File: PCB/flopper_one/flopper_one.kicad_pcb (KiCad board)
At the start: 2 copper layers, 78 x 61 mm, 13 parts, among them J1 To PN532 ->, J2 <- ST7789, Q1 2N2219, SW1 SW_Omron_B3FS, SW2 SW_Omron_B3FS, SW3 SW_Omron_B3FS, SW4 SW_Omron_B3FS, SW5 SW_Omron_B3FS

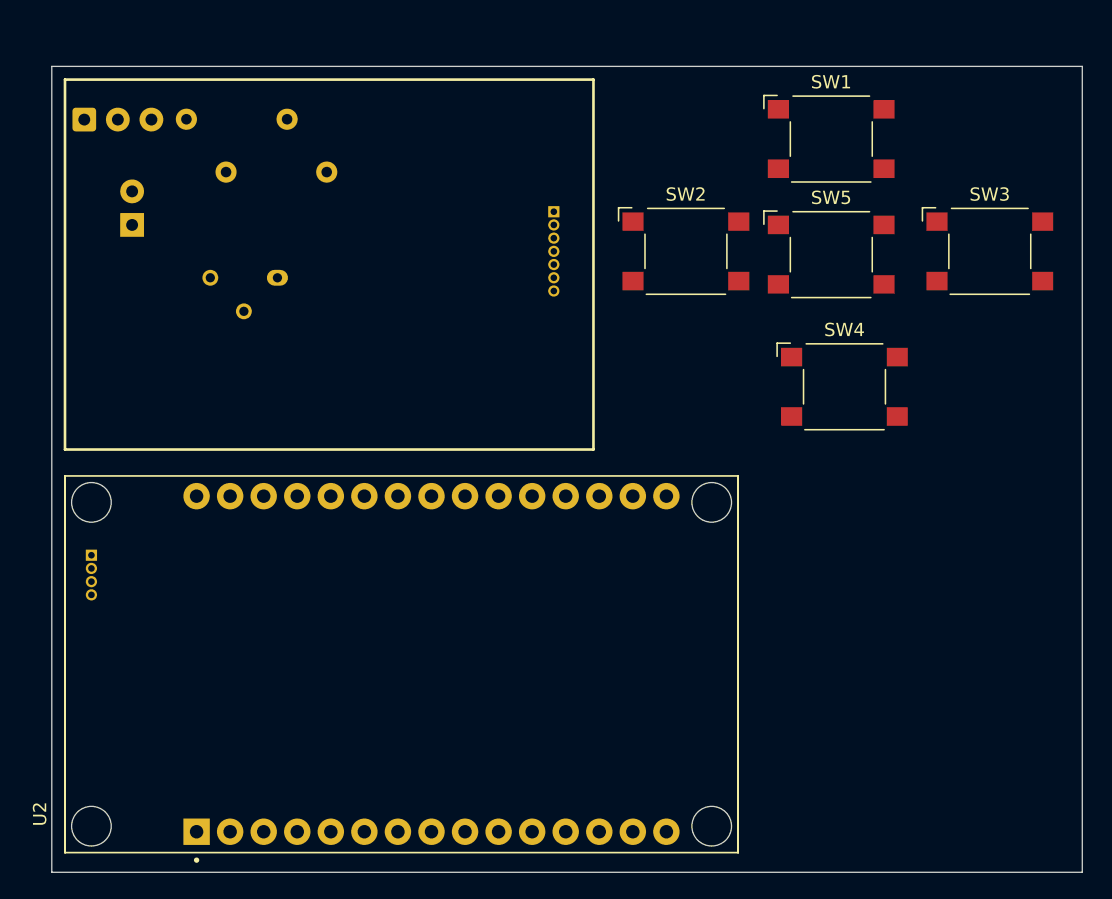
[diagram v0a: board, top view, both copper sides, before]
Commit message: routed switches
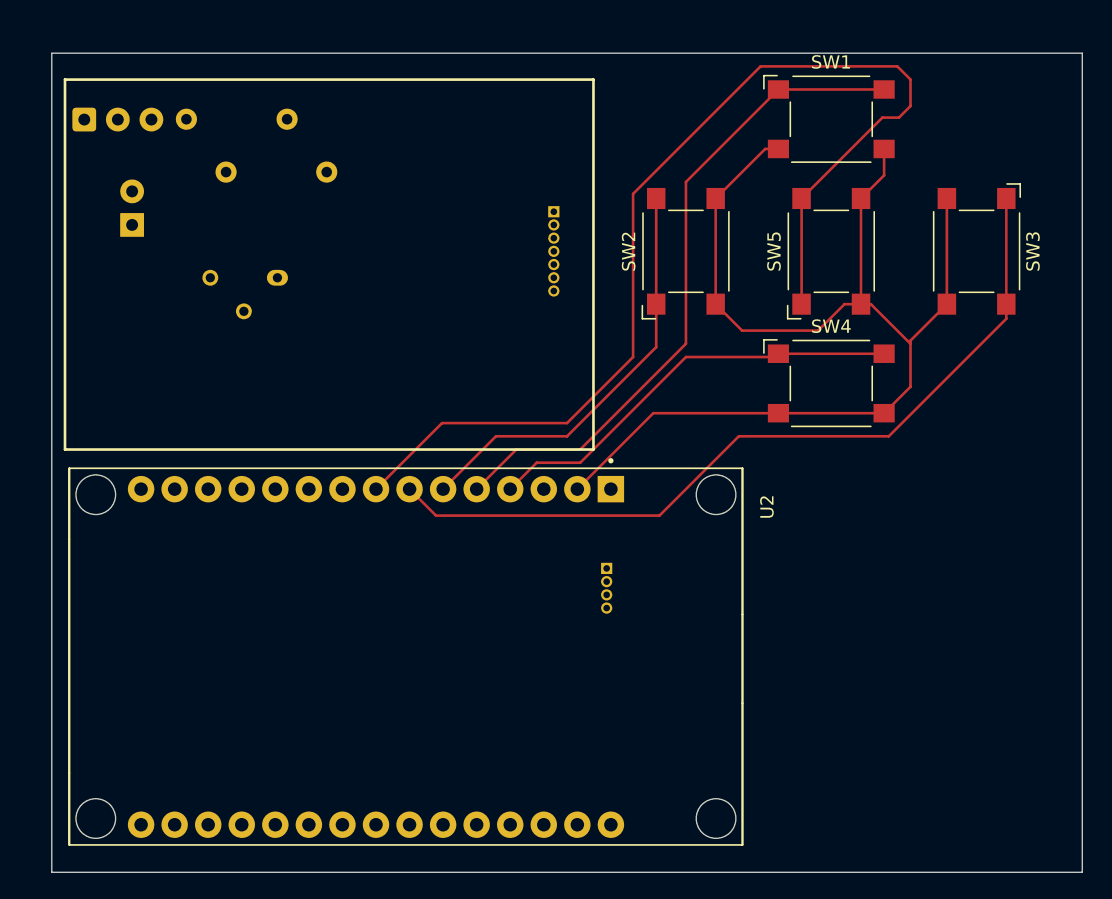
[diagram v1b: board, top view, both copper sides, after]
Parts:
- moved J1 39.0 mm to (185.0, 101.0)
- moved SW1 1.50 mm to (202.0, 67.0)
- moved SW4 1.03 mm to (202.0, 87.0)
- moved SW3 1.00 mm to (213.0, 77.0), turned to -90 degrees
- moved U2 0.62 mm to (169.8, 107.7), turned to -90 degrees
- moved SW5 0.25 mm to (202.0, 77.0), turned to 90 degrees
- turned SW2 to 90 degrees
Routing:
- net GND: track 0.00 -> 88.2 mm
- net Net-(U2-GPIO25): track 0.00 -> 82.5 mm
- net Net-(U2-GPIO26): track 0.00 -> 61.3 mm
- net Net-(U2-GPIO14): track 0.00 -> 50.5 mm
- net Net-(U2-GPIO12): track 0.00 -> 32.5 mm
- net Net-(U2-GPIO27): track 0.00 -> 31.8 mm
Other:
- board size 78 x 61 mm -> 78 x 62 mm

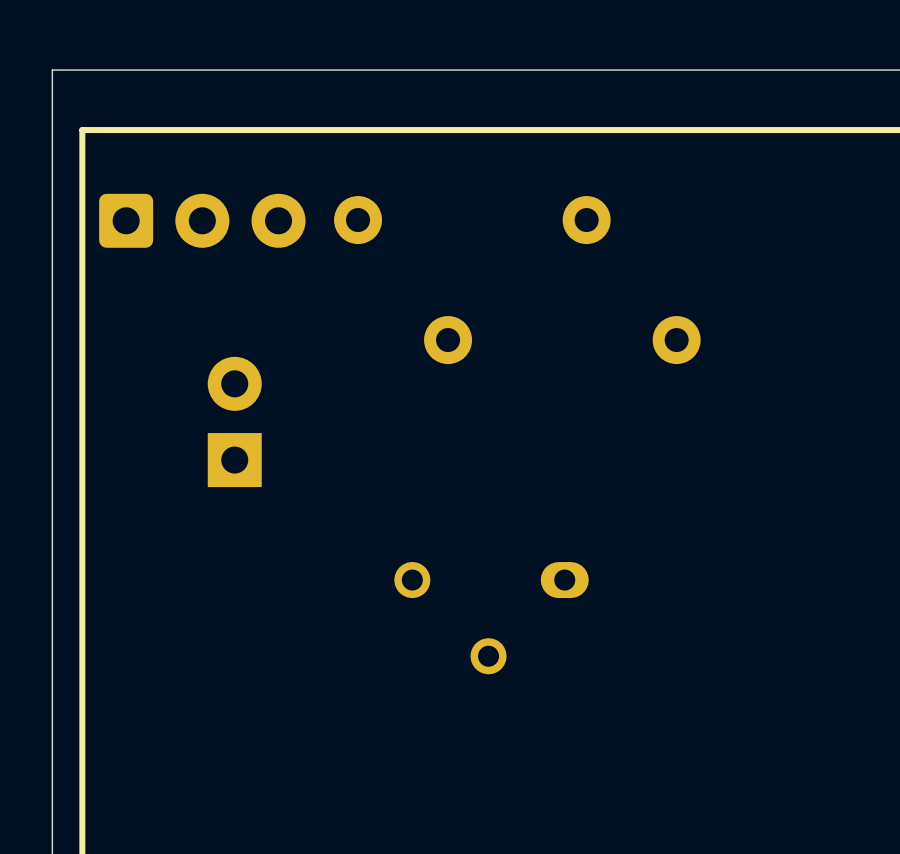
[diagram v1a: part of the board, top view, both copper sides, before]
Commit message: start routing ir
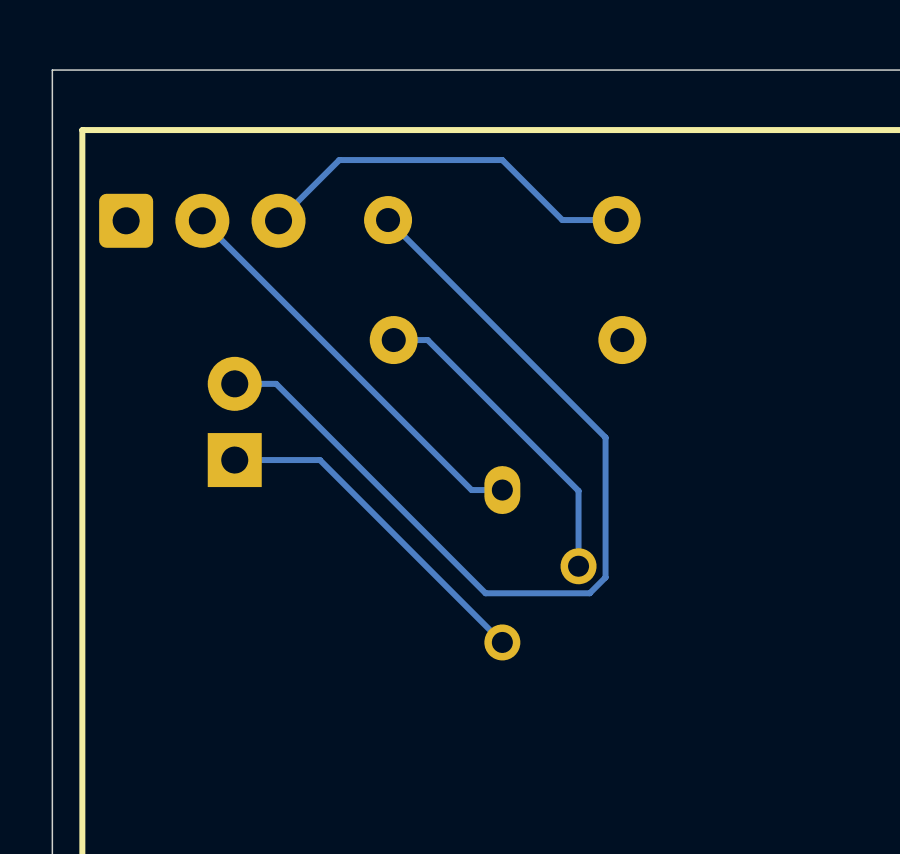
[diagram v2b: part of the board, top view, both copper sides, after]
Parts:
- moved R2 9.43 mm to (154.4, 71.0), turned to 0 degrees
- moved R1 6.62 mm to (154.2, 67.0), turned to 0 degrees
- moved Q1 3.65 mm to (158.0, 76.0), turned to -90 degrees
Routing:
- net Net-(D1-A): track 0.00 -> 30.4 mm
- net GND: track 88.2 -> 102.0 mm
- net /VCC: track 0.00 -> 12.9 mm
- net Net-(D1-K): track 0.00 -> 11.4 mm
- net Net-(Q1-B): track 0.00 -> 10.8 mm

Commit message: routed the pcb
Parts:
- J1: footprint Connector_PinHeader_1.00mm:PinHeader_1x04_P1.00mm_Vertical -> Connector_PinHeader_2.54mm:PinHeader_1x04_P2.54mm_Vertical
- J2: footprint Connector_PinHeader_1.00mm:PinHeader_1x07_P1.00mm_Vertical -> Connector_PinHeader_2.54mm:PinHeader_1x07_P2.54mm_Vertical; moved to F.Cu
- moved D1 21.9 mm to (168.5, 65.0), turned to 180 degrees
- moved Q1 13.3 mm to (170.5, 71.5)
- moved R2 9.62 mm to (164.0, 71.0), turned to 180 degrees
- moved J2 6.40 mm to (185.0, 69.0), turned to 0 degrees
- moved J1 3.00 mm to (185.0, 98.0)
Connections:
- net Net-(U2-GPIO12) renamed /P4
- net Net-(U2-GPIO14) renamed /P1
- net Net-(U2-GPIO25) renamed /P5
- net Net-(U2-GPIO26) renamed /P3
- net Net-(U2-GPIO27) renamed /P2
- J1 pad 3: /SDA -> /SDA1
- J1 pad 4: /SCL -> /SCL1
- J2 pad 3: /SCL -> /SCL2
- J2 pad 4: /SDA -> /SDA2
- U2 pad 22: /SDA -> /SDA1
- U2 pad 23: /SCL -> /SCL1
- U2 pad 24: /SCL -> /SCL2
- U2 pad 25: /SDA -> /SDA2
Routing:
- net /VCC: track 12.9 -> 172.1 mm
- net Net-(U2-GPIO23): track 0.00 -> 105.5 mm
- net GND: track 102.0 -> 191.4 mm
- net Net-(U2-GPIO16): track 0.00 -> 73.0 mm
- net /SCL2: track 0.00 -> 62.8 mm
- net /SDA2: track 0.00 -> 57.1 mm
- net /SDA1: track 0.00 -> 27.2 mm
- net /SCL1: track 0.00 -> 23.6 mm
- net Net-(D1-A): track 30.4 -> 17.2 mm
- net Net-(Q1-B): track 10.8 -> 23.7 mm
- net Net-(D1-K): track 11.4 -> 12.3 mm
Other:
- board size 78 x 62 mm -> 77 x 62 mm
- board text added: "ESP HERE"
- board text added: "IR RECV"
- board text added: "IR SEND"
- board text added: "P1"
- board text added: "P2"
- board text added: "P3"
- board text added: "P4"
- board text added: "P5"
- board text added: "PN532 HERE"
- board text added: "PN532 SCL"
- board text added: "PN532 SDA"
- board text added: "SCREEN HERE"
- board text added: "SCREEN SCL"
- board text added: "SCREEN SDA"

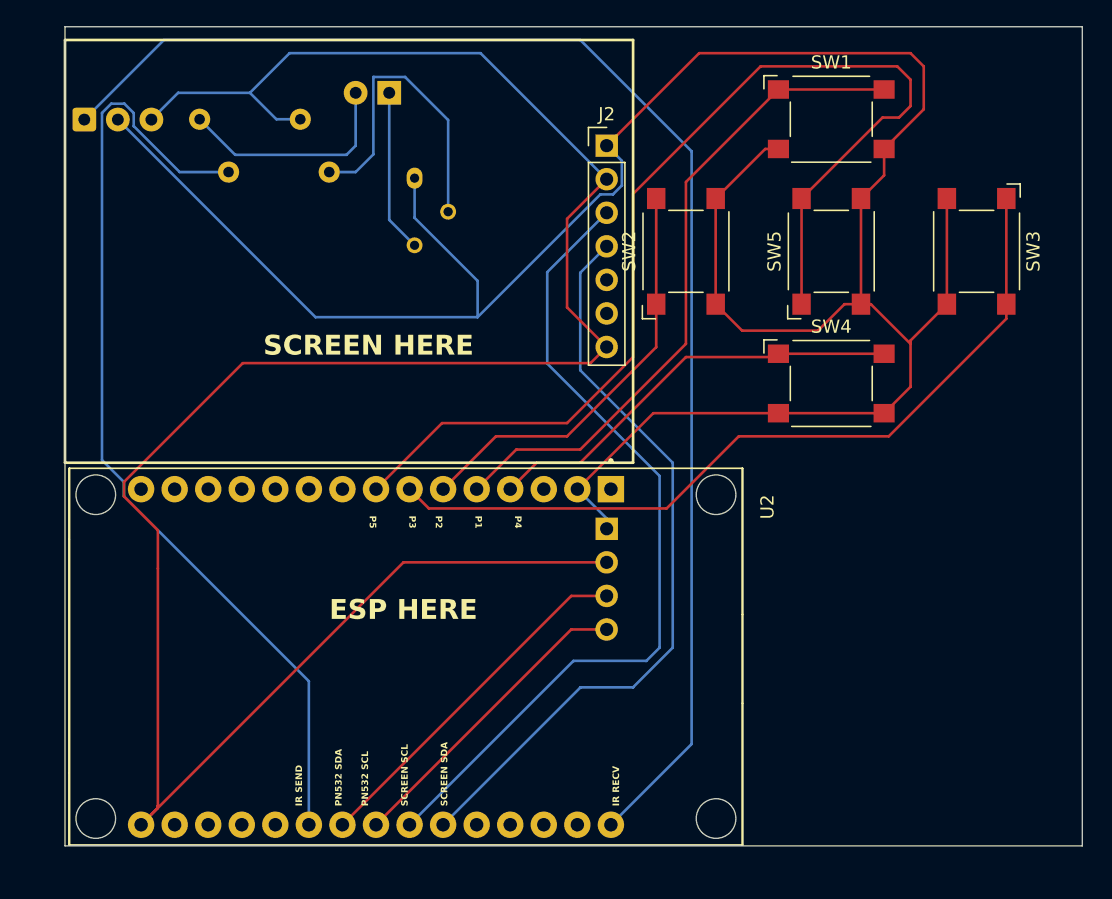
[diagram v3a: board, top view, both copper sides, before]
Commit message: add battery
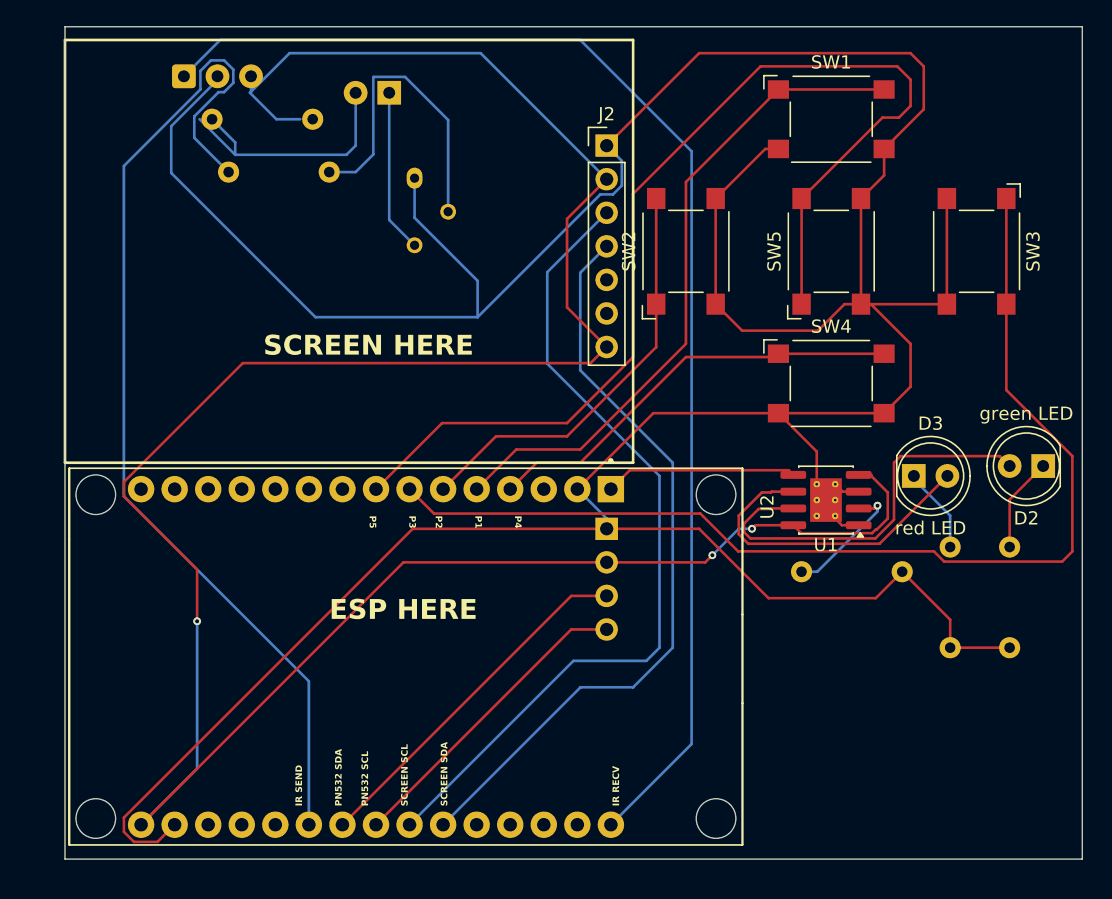
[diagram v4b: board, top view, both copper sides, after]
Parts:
- added D2: green LED, LED_THT:LED_D5.0mm, F.Cu at (218.0, 93.2)
- added D3: red LED, LED_THT:LED_D5.0mm, F.Cu at (208.2, 94.0)
- added R3: 1.2kΩ, Resistor_THT:R_Axial_DIN0207_L6.3mm_D2.5mm_P7.62mm_Horizontal, B.Cu at (199.8, 101.2)
- added R4: 1kΩ, Resistor_THT:R_Axial_DIN0207_L6.3mm_D2.5mm_P7.62mm_Horizontal, B.Cu at (211.0, 107.0)
- added R5: 1kΩ, Resistor_THT:R_Axial_DIN0207_L6.3mm_D2.5mm_P7.62mm_Horizontal, B.Cu at (215.5, 107.0)
- added U1: TP4056-42-ESOP8, Package_SO:SOIC-8-1EP_3.9x4.9mm_P1.27mm_EP2.41x3.3mm_ThermalVias, F.Cu at (201.6, 95.8)
- moved U_2 8.22 mm to (153.0, 63.8)
- moved R1 0.94 mm to (155.1, 67.0)
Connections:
- U2 pad 1: unconnected-(U2-VIN-Pad1) -> /BAT+
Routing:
- net GND: track 191.4 -> 303.1 mm
- net Net-(D2-A): track 0.00 -> 30.6 mm
- net Net-(D3-A): track 0.00 -> 24.5 mm
- net /VCC: track 172.1 -> 196.4 mm, vias 0 -> 3
- net /P3: track 60.8 -> 81.5 mm
- net /BAT+: track 0.00 -> 14.5 mm
- net Net-(U1-PROG): track 0.00 -> 9.59 mm, vias 0 -> 1
- net Net-(U2-GPIO23): track 105.5 -> 96.6 mm
- net Net-(D2-K): track 0.00 -> 7.18 mm
- net Net-(D3-K): track 0.00 -> 6.52 mm
- net Net-(U2-GPIO16): track 73.0 -> 78.7 mm
- net Net-(D1-A): track 17.2 -> 20.6 mm
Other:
- board size 77 x 62 mm -> 77 x 63 mm
- board text added: "1.2kΩ"
- board text added: "1kΩ"
- board text added: "47-100Ω"

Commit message: added like power circuits fr
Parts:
- added C1: 10uf, Capacitor_THT:CP_Axial_L10.0mm_D4.5mm_P15.00mm_Horizontal, B.Cu at (192.8, 91.0)
- added U3: hw-045, MT3608:hw-045, B.Cu at (205.2, 104.0)
- D2, D3: moved to B.Cu
- moved D3 24.2 mm to (218.2, 116.0), turned to 180 degrees
- moved R4 23.0 mm to (218.2, 85.1), turned to -90 degrees
- moved R5 21.9 mm to (215.0, 85.1), turned to -90 degrees
- moved R3 17.6 mm to (216.2, 95.2), turned to -90 degrees
- moved D2 15.5 mm to (218.0, 108.8)
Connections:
- D2 pad 2: Net-(D2-A) -> GND
- D3 pad 2: Net-(D3-A) -> GND
- R4 pad 1: GND -> Net-(U1-~{STDBY})
- R5 pad 1: GND -> Net-(U1-~{CHRG})
- U1 pad 6: Net-(D3-A) -> Net-(U1-~{STDBY})
- U1 pad 7: Net-(D2-A) -> Net-(U1-~{CHRG})
- U2 pad 1: /BAT+ -> /VIN
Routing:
- net /VIN: track 0.00 -> 40.8 mm, vias 0 -> 1
- net GND: track 303.1 -> 342.7 mm, vias 0 -> 1
- net Net-(U1-~{STDBY}): track 0.00 -> 37.3 mm
- net Net-(U1-~{CHRG}): track 0.00 -> 33.3 mm
- net Net-(D2-A): track 30.6 -> 0.00 mm
- net Net-(D3-A): track 24.5 -> 0.00 mm
- net Net-(D3-K): track 6.52 -> 24.5 mm
- net /BAT+: track 14.5 -> 31.1 mm, vias 0 -> 1
- net Net-(D2-K): track 7.18 -> 18.7 mm
- net Net-(D1-A): track 20.6 -> 16.8 mm
- net Net-(U1-PROG): track 9.59 -> 12.7 mm
- net /P3: track 81.5 -> 80.1 mm
- net /VCC: track 196.4 -> 197.5 mm
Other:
- board text added: "10uf"
- board text added: "BAT+"
- board text added: "BAT-"

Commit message: fix battery rq
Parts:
- removed U3: hw-045, MT3608:hw-045
- added U4: hw-045, MT3608:hw-045, B.Cu at (204.2, 104.2)
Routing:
- net GND: track 342.7 -> 332.5 mm
- net /BAT+: track 31.1 -> 33.6 mm
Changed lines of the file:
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@@
 	(footprint "MT3608:hw-045"
 		(layer "B.Cu")
-		(at 205.25 104 -90)
-		(property "Reference" "U3"
+		(at 204.15 104.25 90)
+		(property "Reference" "U4"
 			(at 0 -0.5 90)
 			(layer "B.SilkS")
@@
 		(attr through_hole)
 		(fp_line
-			(start -17.3 9)
-			(end 17.7 9)
+			(start 17.7 -8)
+			(end 18.7 -7)
 			(stroke
 				(width 0.12)
@@
 		)
 		(fp_line
-			(start -18.3 8)
-			(end -17.3 9)
+			(start -17.3 -8)
+			(end 17.7 -8)
 			(stroke
 				(width 0.12)
@@
 		)
 		(fp_line
-			(start 18.7 8)
-			(end 17.7 9)
+			(start 18.7 -7)
+			(end 18.7 8)
 			(stroke
 				(width 0.12)
@@
 		(fp_line
 			(start -18.3 -7)
-			(end -18.3 8)
+			(end -17.3 -8)
 			(stroke
 				(width 0.12)
@@
 		(fp_line
 			(start -18.3 -7)
-			(end -17.3 -8)
+			(end -18.3 8)
 			(stroke
 				(width 0.12)
@@
 		)
 		(fp_line
-			(start 18.7 -7)
-			(end 18.7 8)
+			(start 18.7 8)
+			(end 17.7 9)
 			(stroke
 				(width 0.12)
@@
 		)
 		(fp_line
-			(start -17.3 -8)
-			(end 17.7 -8)
+			(start -18.3 8)
+			(end -17.3 9)
 			(stroke
 				(width 0.12)
@@
 		)
 		(fp_line
-			(start 17.7 -8)
-			(end 18.7 -7)
+			(start -17.3 9)
+			(end 17.7 9)
 			(stroke
 				(width 0.12)
@@
 		)
 		(pad "1" smd roundrect
-			(at -15 -2.9 270)
+			(at -15 -2.9 90)
 			(size 5 3)
 			(layers "B.Cu" "B.Mask" "B.Paste")
 			(roundrect_rratio 0.25)
-			(net 39 "/BAT+")
-			(pinfunction "VIN+")
+			(net 40 "/VIN")
+			(pinfunction "VOUT+")
 			(pintype "input")
 		)
 		(pad "2" smd roundrect
-			(at -15 3.9 270)
+			(at -15 3.9 90)
 			(size 5 3)
 			(layers "B.Cu" "B.Mask" "B.Paste")
 			(roundrect_rratio 0.25)
 			(net 3 "GND")
-			(pinfunction "VIN-")
+			(pinfunction "VOUT-")
 			(pintype "input")
 		)
 		(pad "3" smd roundrect
-			(at 15.5 3.9 270)
+			(at 15.5 3.9 90)
 			(size 5 3)
 			(layers "B.Cu" "B.Mask" "B.Paste")
 			(roundrect_rratio 0.25)
-			(net 40 "/VIN")
-			(pinfunction "VOUT+")
+			(net 3 "GND")
+			(pinfunction "VIN-")
 			(pintype "input")
 		)
 		(pad "4" smd roundrect
-			(at 15.5 -2.9 270)
+			(at 15.5 -2.9 90)
 			(size 5 3)
 			(layers "B.Cu" "B.Mask" "B.Paste")
 			(roundrect_rratio 0.25)
-			(net 3 "GND")
-			(pinfunction "VOUT-")
+			(net 39 "/BAT+")
+			(pinfunction "VIN+")
 			(pintype "input")
 		)
@@
 		(fill yes)
 		(layer "B.Cu")
-		(net 3)
+		(net 39)
 	)
 	(gr_rect
@@
 	)
 	(segment
-		(start 198 91.25)
-		(end 198 89.25)
-		(width 0.2)
-		(layer "F.Cu")
-		(net 3)
-	)
-	(segment
 		(start 209 63)
 		(end 208 62)
@@
 	)
 	(segment
-		(start 198.25 91.5)
-		(end 198 91.25)
-		(width 0.2)
-		(layer "F.Cu")
-		(net 3)
-	)
-	(segment
 		(start 203 81)
 		(end 204.25 81)
@@
 	)
 	(segment
+		(start 206 89.25)
+		(end 206 87.75)
+		(width 0.2)
+		(layer "F.Cu")
+		(net 3)
+	)
+	(segment
 		(start 200.9 97.025)
 		(end 202.3 97.025)
@@
 	)
 	(via
-		(at 198.25 91.5)
+		(at 206 87.75)
 		(size 0.6)
 		(drill 0.3)
@@
 	)
 	(segment
-		(start 198.5 82.5)
-		(end 198.5 83)
-		(width 0.2)
-		(layer "B.Cu")
-		(net 3)
-	)
-	(segment
 		(start 215.71 117.79)
 		(end 214 119.5)
@@
 	)
 	(segment
-		(start 198.85 91.5)
-		(end 198.25 91.5)
-		(width 0.2)
-		(layer "B.Cu")
-		(net 3)
-	)
-	(segment
 		(start 208.15 119.5)
 		(end 214 119.5)
@@
 	)
 	(segment
-		(start 201.35 89)
-		(end 198.85 91.5)
-		(width 0.2)
-		(layer "B.Cu")
-		(net 3)
-	)
-	(segment
 		(start 162.956 81.981)
 		(end 152.04 71.065)
@@
 	)
 	(segment
+		(start 207.05 87.75)
+		(end 208.05 88.75)
+		(width 0.2)
+		(layer "B.Cu")
+		(net 3)
+	)
+	(segment
 		(start 215.71 102.85)
 		(end 215.71 108.5)
@@
 	)
 	(segment
-		(start 198.5 83)
-		(end 201.35 85.85)
-		(width 0.2)
-		(layer "B.Cu")
-		(net 3)
-	)
-	(segment
 		(start 175.23324 81.981)
 		(end 184.52324 72.691)
@@
 	)
 	(segment
-		(start 201.35 85.85)
-		(end 201.35 89)
+		(start 206 87.75)
+		(end 207.05 87.75)
 		(width 0.2)
 		(layer "B.Cu")
@@
 	)
 	(segment
-		(start 204.15 93)
-		(end 208.15 89)
+		(start 198.5 82.5)
+		(end 198.5 83)
+		(width 0.2)
+		(layer "B.Cu")
+		(net 39)
+	)
+	(segment
+		(start 199.499999 93)
+		(end 201.25 91.249999)
+		(width 0.2)
+		(layer "B.Cu")
+		(net 39)
+	)
+	(segment
+		(start 201.25 88.75)
+		(end 201.25 85.25)
 		(width 0.2)
 		(layer "B.Cu")
@@
 	(segment
 		(start 197.5 93)
-		(end 204.15 93)
+		(end 199.499999 93)
+		(width 0.2)
+		(layer "B.Cu")
+		(net 39)
+	)
+	(segment
+		(start 201.25 85.25)
+		(end 198.5 82.5)
 		(width 0.2)
 		(layer "B.Cu")
@@
 		(width 0.2)
 		(layer "B.Cu")
+		(net 39)
+	)
+	(segment
+		(start 201.25 91.249999)
+		(end 201.25 88.75)
+		(width 0.2)
+		(layer "B.Cu")
